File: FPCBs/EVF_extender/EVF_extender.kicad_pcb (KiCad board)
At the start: 2 copper layers, 23.9 x 22.7 mm, 2 parts, among them J3 FR02C061JA1-R5000, J4 FPC_2Rows-61Pins_0.2mm

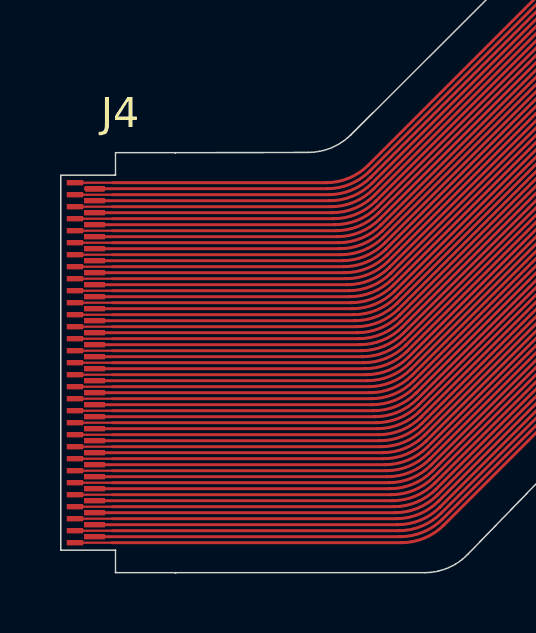
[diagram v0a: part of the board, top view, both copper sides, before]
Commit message: Move leds to Right board
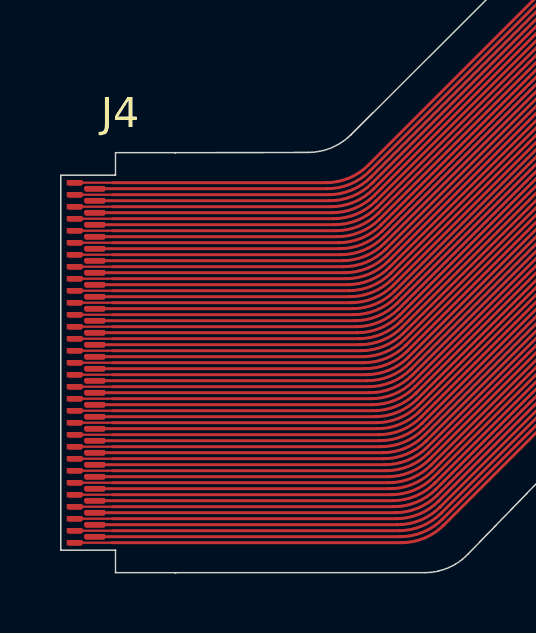
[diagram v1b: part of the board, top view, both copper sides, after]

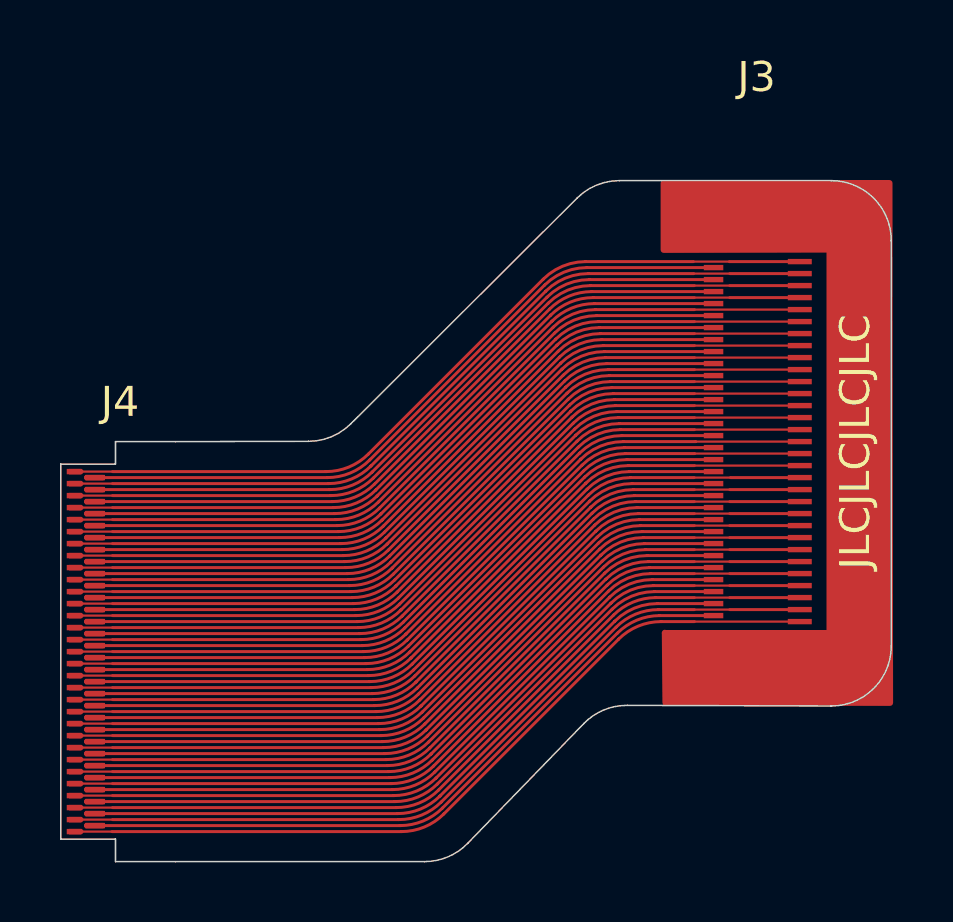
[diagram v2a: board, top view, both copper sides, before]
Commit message: Add back copper
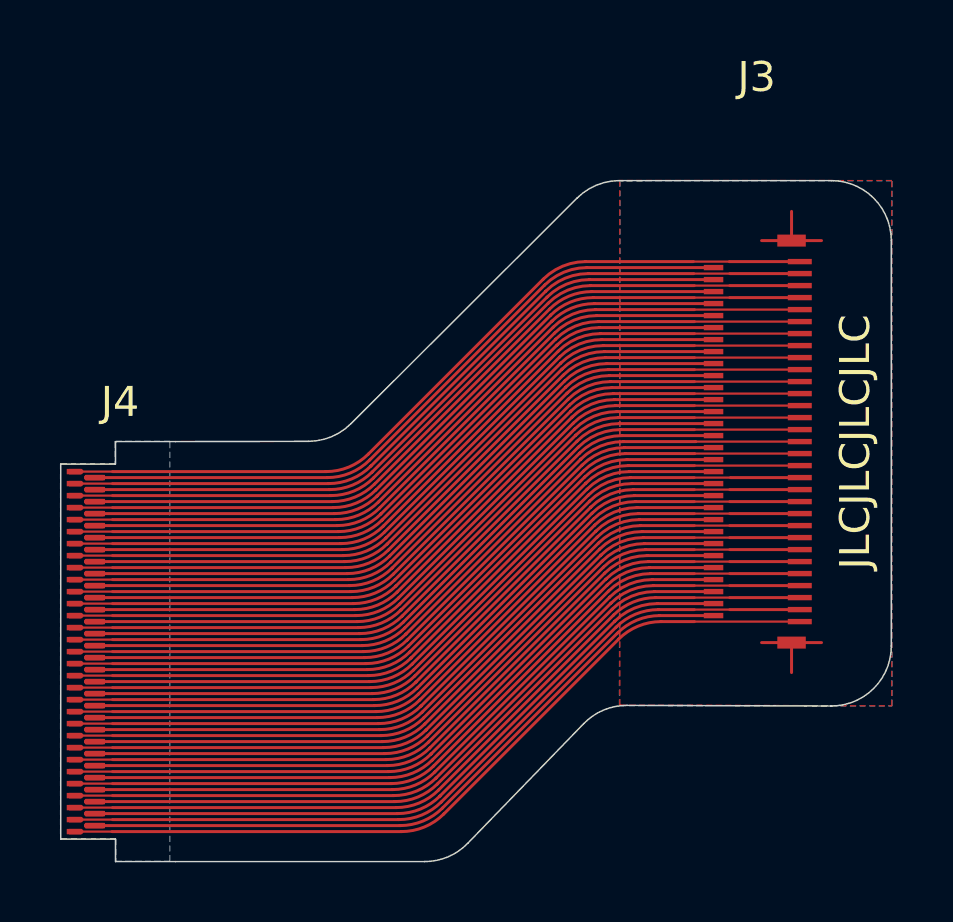
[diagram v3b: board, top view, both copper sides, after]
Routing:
- net (no net): track 0.00 -> 5.90 mm
- added copper zone on B.Cu, net (none)
- added copper zone on F.Cu, net (none)
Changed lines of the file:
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@@
 			(pinfunction "1")
 			(pintype "passive")
-			(solder_mask_margin 0.01)
-			(clearance 0.01)
 		)
 		(pad "2" smd rect
@@
 			(pinfunction "3")
 			(pintype "passive")
-			(solder_mask_margin 0.01)
-			(clearance 0.01)
 		)
 		(pad "4" smd rect
@@
 			(pinfunction "5")
 			(pintype "passive")
-			(solder_mask_margin 0.01)
-			(clearance 0.01)
 		)
 		(pad "6" smd rect
@@
 		(embedded_fonts no)
 	)
-	(gr_poly
-		(pts
-			(xy 152.51 84.38) (xy 158 84.38) (xy 158 71.6) (xy 152.47 71.61) (xy 152.47 69.38) (xy 160 69.38)
-			(xy 160.02 86.71) (xy 152.53 86.7) (xy 152.51 84.37)
-		)
-		(stroke
-			(width 0.2)
-			(type solid)
-		)
-		(fill yes)
-		(layer "F.Cu")
-	)
 	(gr_line
 		(start 160.06 84.813779)
@@
 	)
 	(segment
+		(start 156.735 84.7)
+		(end 157.735 84.7)
+		(width 0.1)
+		(layer "F.Cu")
+		(net 0)
+	)
+	(segment
+		(start 156.735 84.7)
+		(end 155.735 84.7)
+		(width 0.1)
+		(layer "F.Cu")
+		(net 0)
+	)
+	(segment
+		(start 156.735 71.3)
+		(end 155.735 71.3)
+		(width 0.1)
+		(layer "F.Cu")
+		(net 0)
+	)
+	(segment
+		(start 156.735 84.7)
+		(end 156.735 85.7)
+		(width 0.1)
+		(layer "F.Cu")
+		(net 0)
+	)
+	(segment
+		(start 156.735 71.225)
+		(end 156.735 70.325)
+		(width 0.1)
+		(layer "F.Cu")
+		(net 0)
+	)
+	(segment
+		(start 156.735 71.3)
+		(end 157.735 71.3)
+		(width 0.1)
+		(layer "F.Cu")
+		(net 0)
+	)
+	(segment
 		(start 132.85 82.6)
 		(end 134.1 82.6)
@@
 		(net 61)
 	)
+	(zone
+		(net 0)
+		(net_name "")
+		(layer "F.Cu")
+		(hatch edge 0.5)
+		(connect_pads
+			(clearance 0.5)
+		)
+		(min_thickness 0.25)
+		(filled_areas_thickness no)
+		(fill yes
+			(thermal_gap 0.5)
+			(thermal_bridge_width 0.5)
+			(island_removal_mode 1)
+			(island_area_min 10)
+		)
+		(polygon
+			(pts
+				(xy 151.01 69.3) (xy 151.01 86.78) (xy 160.07 86.81) (xy 160.08 86.8) (xy 160.08 69.3)
+			)
+		)
+	)
+	(zone
+		(net 0)
+		(net_name "")
+		(layer "B.Cu")
+		(hatch edge 0.5)
+		(connect_pads
+			(clearance 0.5)
+		)
+		(min_thickness 0.25)
+		(filled_areas_thickness no)
+		(fill yes
+			(thermal_gap 0.5)
+			(thermal_bridge_width 0.5)
+			(island_removal_mode 1)
+			(island_area_min 10)
+		)
+		(polygon
+			(pts
+				(xy 151.01 69.31) (xy 151 86.8) (xy 160.07 86.81) (xy 160.08 86.8) (xy 160.08 69.3)
+			)
+		)
+	)
+	(zone
+		(net 0)
+		(net_name "")
+		(layer "B.Cu")
+		(hatch edge 0.5)
+		(priority 1)
+		(connect_pads
+			(clearance 0.5)
+		)
+		(min_thickness 0.25)
+		(filled_areas_thickness no)
+		(fill yes
+			(thermal_gap 0.5)
+			(thermal_bridge_width 0.5)
+			(island_removal_mode 1)
+			(island_area_min 10)
+		)
+		(polygon
+			(pts
+				(xy 136.01 77.99) (xy 134.19 77.99) (xy 134.18 78) (xy 134.18 78.74) (xy 132.37 78.74) (xy 132.37 91.21)
+				(xy 132.4 91.24) (xy 134.2 91.24) (xy 134.21 91.25) (xy 134.21 91.98) (xy 134.22 91.99) (xy 136 91.99)
+				(xy 136.01 91.98)
+			)
+		)
+	)
 	(embedded_fonts no)

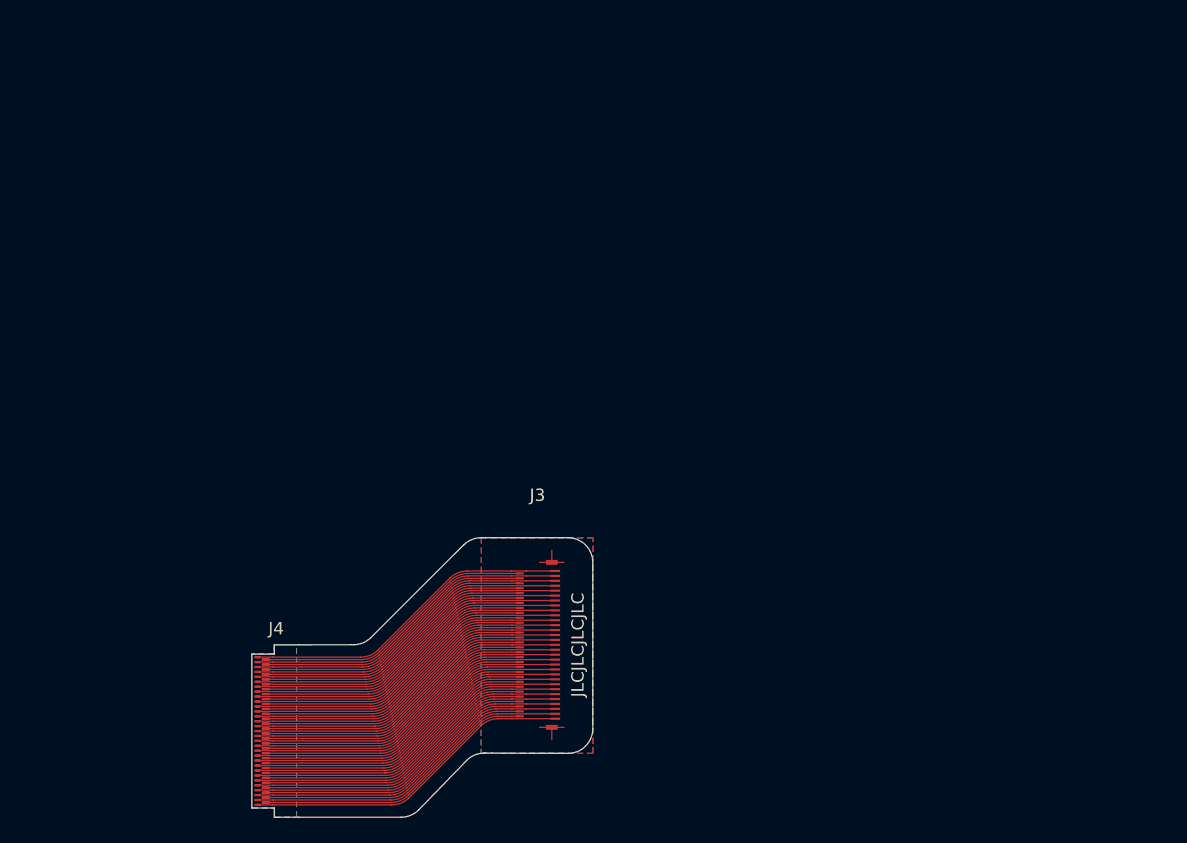
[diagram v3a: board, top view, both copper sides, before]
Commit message: Rewire one side of the evf connector to the back side
Add Lumix logo
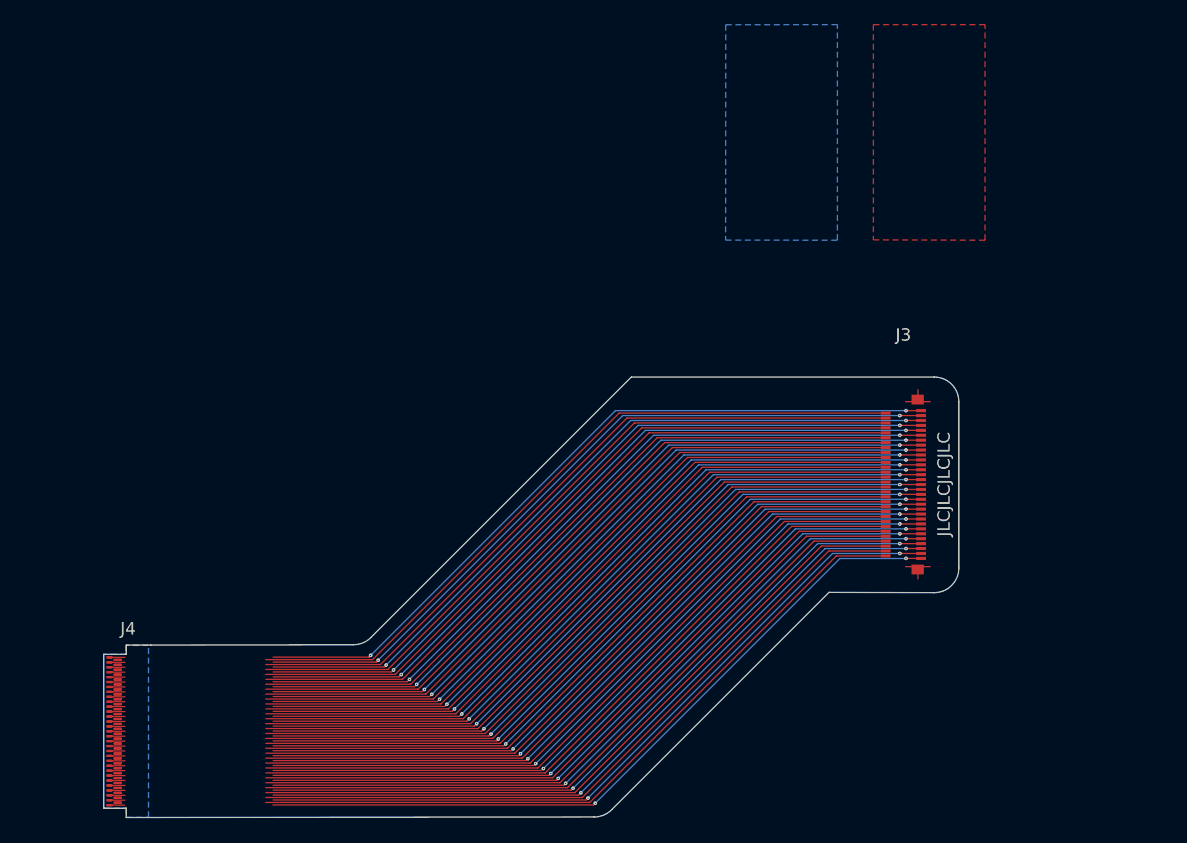
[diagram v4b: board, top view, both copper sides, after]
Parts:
- moved J3 32.4 mm to (185.2, 65.0)
- moved J4 12.0 mm to (122.2, 85.0)
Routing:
- net Net-(J4-Pin_6): track 23.3 -> 58.6 mm
- net Net-(J4-Pin_8): track 23.3 -> 58.6 mm
- net Net-(J4-Pin_58): track 23.3 -> 58.6 mm
- net Net-(J4-Pin_53): track 26.9 -> 62.2 mm, vias 0 -> 2
- net Net-(J4-Pin_48): track 23.3 -> 58.6 mm
- net Net-(J4-Pin_28): track 23.3 -> 58.6 mm
- net Net-(J4-Pin_38): track 23.3 -> 58.6 mm
- net Net-(J4-Pin_47): track 26.9 -> 62.2 mm, vias 0 -> 2
- net Net-(J4-Pin_45): track 26.9 -> 62.2 mm, vias 0 -> 2
- net Net-(J4-Pin_26): track 23.3 -> 58.6 mm
- net Net-(J4-Pin_22): track 23.3 -> 58.6 mm
- net Net-(J4-Pin_2): track 23.3 -> 58.6 mm
- net Net-(J4-Pin_18): track 23.3 -> 58.6 mm
- net Net-(J4-Pin_17): track 26.9 -> 62.2 mm, vias 0 -> 2
- net Net-(J4-Pin_16): track 23.3 -> 58.6 mm
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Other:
- board size 23.9 x 22.7 mm -> 65.6 x 35.8 mm

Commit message: Correct evf distance
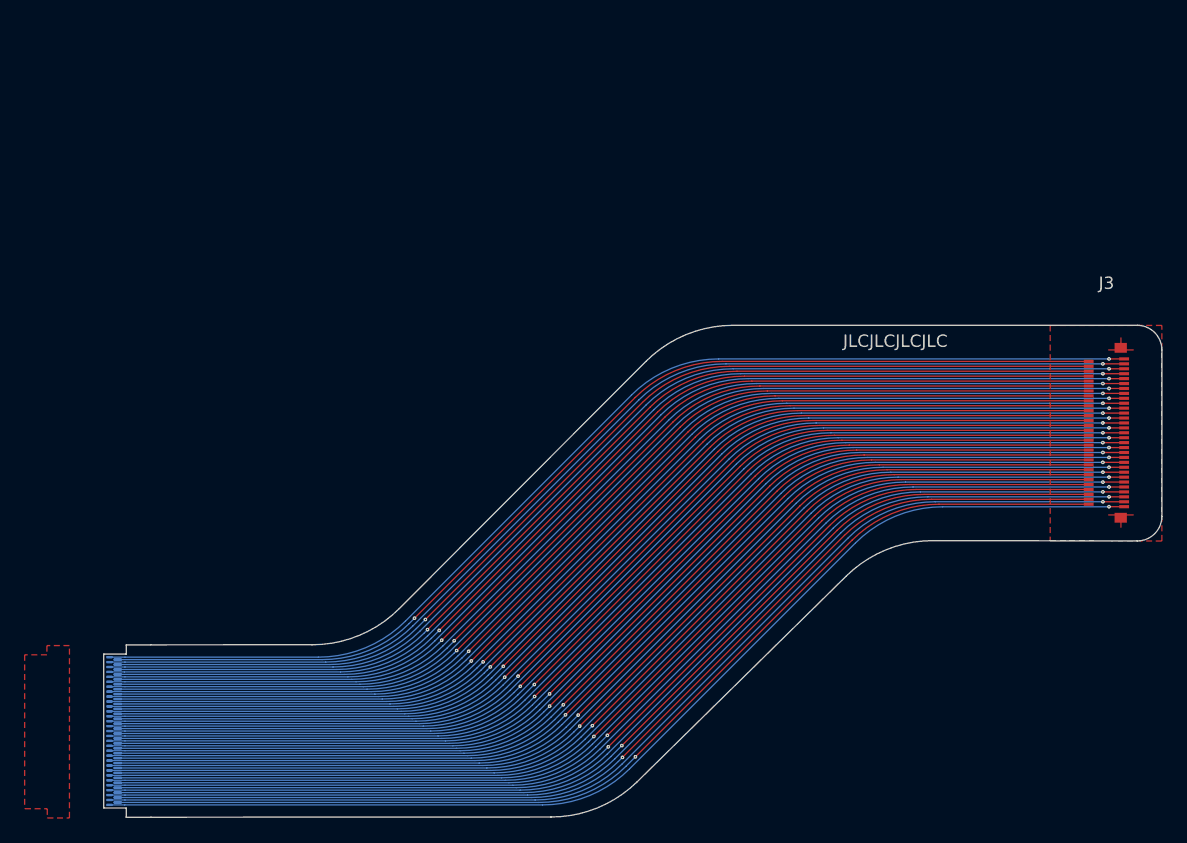
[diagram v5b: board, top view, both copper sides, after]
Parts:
- J4: moved to B.Cu
- moved J3 17.0 mm to (201.7, 60.8)
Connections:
- J3 pad 1: Net-(J4-Pin_61) -> Net-(J4-Pin_1)
- J3 pad 10: Net-(J4-Pin_52) -> Net-(J4-Pin_10)
- J3 pad 11: Net-(J4-Pin_51) -> Net-(J4-Pin_11)
- J3 pad 12: Net-(J4-Pin_50) -> Net-(J4-Pin_12)
- J3 pad 13: Net-(J4-Pin_49) -> Net-(J4-Pin_13)
- J3 pad 14: Net-(J4-Pin_48) -> Net-(J4-Pin_14)
- J3 pad 15: Net-(J4-Pin_47) -> Net-(J4-Pin_15)
- J3 pad 16: Net-(J4-Pin_46) -> Net-(J4-Pin_16)
- J3 pad 17: Net-(J4-Pin_45) -> Net-(J4-Pin_17)
- J3 pad 18: Net-(J4-Pin_44) -> Net-(J4-Pin_18)
- J3 pad 19: Net-(J4-Pin_43) -> Net-(J4-Pin_19)
- J3 pad 2: Net-(J4-Pin_60) -> Net-(J4-Pin_2)
- J3 pad 20: Net-(J4-Pin_42) -> Net-(J4-Pin_20)
- J3 pad 21: Net-(J4-Pin_41) -> Net-(J4-Pin_21)
- J3 pad 22: Net-(J4-Pin_40) -> Net-(J4-Pin_22)
- J3 pad 23: Net-(J4-Pin_39) -> Net-(J4-Pin_23)
- J3 pad 24: Net-(J4-Pin_38) -> Net-(J4-Pin_24)
- J3 pad 25: Net-(J4-Pin_37) -> Net-(J4-Pin_25)
- J3 pad 26: Net-(J4-Pin_36) -> Net-(J4-Pin_26)
- J3 pad 27: Net-(J4-Pin_35) -> Net-(J4-Pin_27)
- J3 pad 28: Net-(J4-Pin_34) -> Net-(J4-Pin_28)
- J3 pad 29: Net-(J4-Pin_33) -> Net-(J4-Pin_29)
- J3 pad 3: Net-(J4-Pin_59) -> Net-(J4-Pin_3)
- J3 pad 30: Net-(J4-Pin_32) -> Net-(J4-Pin_30)
- J3 pad 32: Net-(J4-Pin_30) -> Net-(J4-Pin_32)
- J3 pad 33: Net-(J4-Pin_29) -> Net-(J4-Pin_33)
- J3 pad 34: Net-(J4-Pin_28) -> Net-(J4-Pin_34)
- J3 pad 35: Net-(J4-Pin_27) -> Net-(J4-Pin_35)
- J3 pad 36: Net-(J4-Pin_26) -> Net-(J4-Pin_36)
- J3 pad 37: Net-(J4-Pin_25) -> Net-(J4-Pin_37)
- J3 pad 38: Net-(J4-Pin_24) -> Net-(J4-Pin_38)
- J3 pad 39: Net-(J4-Pin_23) -> Net-(J4-Pin_39)
- J3 pad 4: Net-(J4-Pin_58) -> Net-(J4-Pin_4)
- J3 pad 40: Net-(J4-Pin_22) -> Net-(J4-Pin_40)
- J3 pad 41: Net-(J4-Pin_21) -> Net-(J4-Pin_41)
- J3 pad 42: Net-(J4-Pin_20) -> Net-(J4-Pin_42)
- J3 pad 43: Net-(J4-Pin_19) -> Net-(J4-Pin_43)
- J3 pad 44: Net-(J4-Pin_18) -> Net-(J4-Pin_44)
- J3 pad 45: Net-(J4-Pin_17) -> Net-(J4-Pin_45)
- J3 pad 46: Net-(J4-Pin_16) -> Net-(J4-Pin_46)
- J3 pad 47: Net-(J4-Pin_15) -> Net-(J4-Pin_47)
- J3 pad 48: Net-(J4-Pin_14) -> Net-(J4-Pin_48)
- J3 pad 49: Net-(J4-Pin_13) -> Net-(J4-Pin_49)
- J3 pad 5: Net-(J4-Pin_57) -> Net-(J4-Pin_5)
- J3 pad 50: Net-(J4-Pin_12) -> Net-(J4-Pin_50)
- J3 pad 51: Net-(J4-Pin_11) -> Net-(J4-Pin_51)
- J3 pad 52: Net-(J4-Pin_10) -> Net-(J4-Pin_52)
- J3 pad 53: Net-(J4-Pin_9) -> Net-(J4-Pin_53)
- J3 pad 54: Net-(J4-Pin_8) -> Net-(J4-Pin_54)
- J3 pad 55: Net-(J4-Pin_7) -> Net-(J4-Pin_55)
- J3 pad 56: Net-(J4-Pin_6) -> Net-(J4-Pin_56)
- J3 pad 57: Net-(J4-Pin_5) -> Net-(J4-Pin_57)
- J3 pad 58: Net-(J4-Pin_4) -> Net-(J4-Pin_58)
- J3 pad 59: Net-(J4-Pin_3) -> Net-(J4-Pin_59)
- J3 pad 6: Net-(J4-Pin_56) -> Net-(J4-Pin_6)
- J3 pad 60: Net-(J4-Pin_2) -> Net-(J4-Pin_60)
- J3 pad 61: Net-(J4-Pin_1) -> Net-(J4-Pin_61)
- J3 pad 7: Net-(J4-Pin_55) -> Net-(J4-Pin_7)
- J3 pad 8: Net-(J4-Pin_54) -> Net-(J4-Pin_8)
- J3 pad 9: Net-(J4-Pin_53) -> Net-(J4-Pin_9)
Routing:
- net Net-(J4-Pin_59): track 62.1 -> 91.5 mm, vias 2 -> 1
- net Net-(J4-Pin_61): track 62.1 -> 91.5 mm, vias 2 -> 1
- net Net-(J4-Pin_50): track 58.6 -> 87.9 mm, vias 0 -> 1
- net Net-(J4-Pin_7): track 62.2 -> 91.5 mm, vias 2 -> 1
- net Net-(J4-Pin_36): track 58.6 -> 87.9 mm, vias 0 -> 1
- net Net-(J4-Pin_40): track 58.6 -> 87.9 mm, vias 0 -> 1
- net Net-(J4-Pin_42): track 58.6 -> 87.9 mm, vias 0 -> 1
- net Net-(J4-Pin_34): track 58.6 -> 87.9 mm, vias 0 -> 1
- net Net-(J4-Pin_32): track 58.6 -> 87.9 mm, vias 0 -> 1
- net Net-(J4-Pin_30): track 58.6 -> 87.9 mm, vias 0 -> 1
- net Net-(J4-Pin_16): track 58.6 -> 87.9 mm, vias 0 -> 1
- net Net-(J4-Pin_38): track 58.6 -> 87.9 mm, vias 0 -> 1
- net Net-(J4-Pin_46): track 58.6 -> 87.9 mm, vias 0 -> 1
- net Net-(J4-Pin_8): track 58.6 -> 87.9 mm, vias 0 -> 1
- net Net-(J4-Pin_26): track 58.6 -> 87.9 mm, vias 0 -> 1
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- removed copper zone on B.Cu, net (none)
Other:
- board size 65.6 x 35.8 mm -> 82.1 x 40 mm
